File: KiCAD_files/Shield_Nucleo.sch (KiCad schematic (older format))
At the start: 125 parts, among them J1 Conn_01x02, J2 RJ45_LED_Shielded, J3 RJ45_LED_Shielded, J4 Conn_01x03_Male, J5 Conn_01x05_Male, J6 Conn_01x02, J7 Power, J8 Conn_02x07_Odd_Even, SW1 SW_Push, U1 STM32G474RE, U2 AT25xxx, U3 TCAN334GDR, U4 AP1117-33, U5 UCC21222DR, U6 UCC21222DR, U7 SFH617A-2X009T, U8 RFM-0505s, U9 RFM-0505s, Y1 NX3225SA-16.000000MHZ-T1

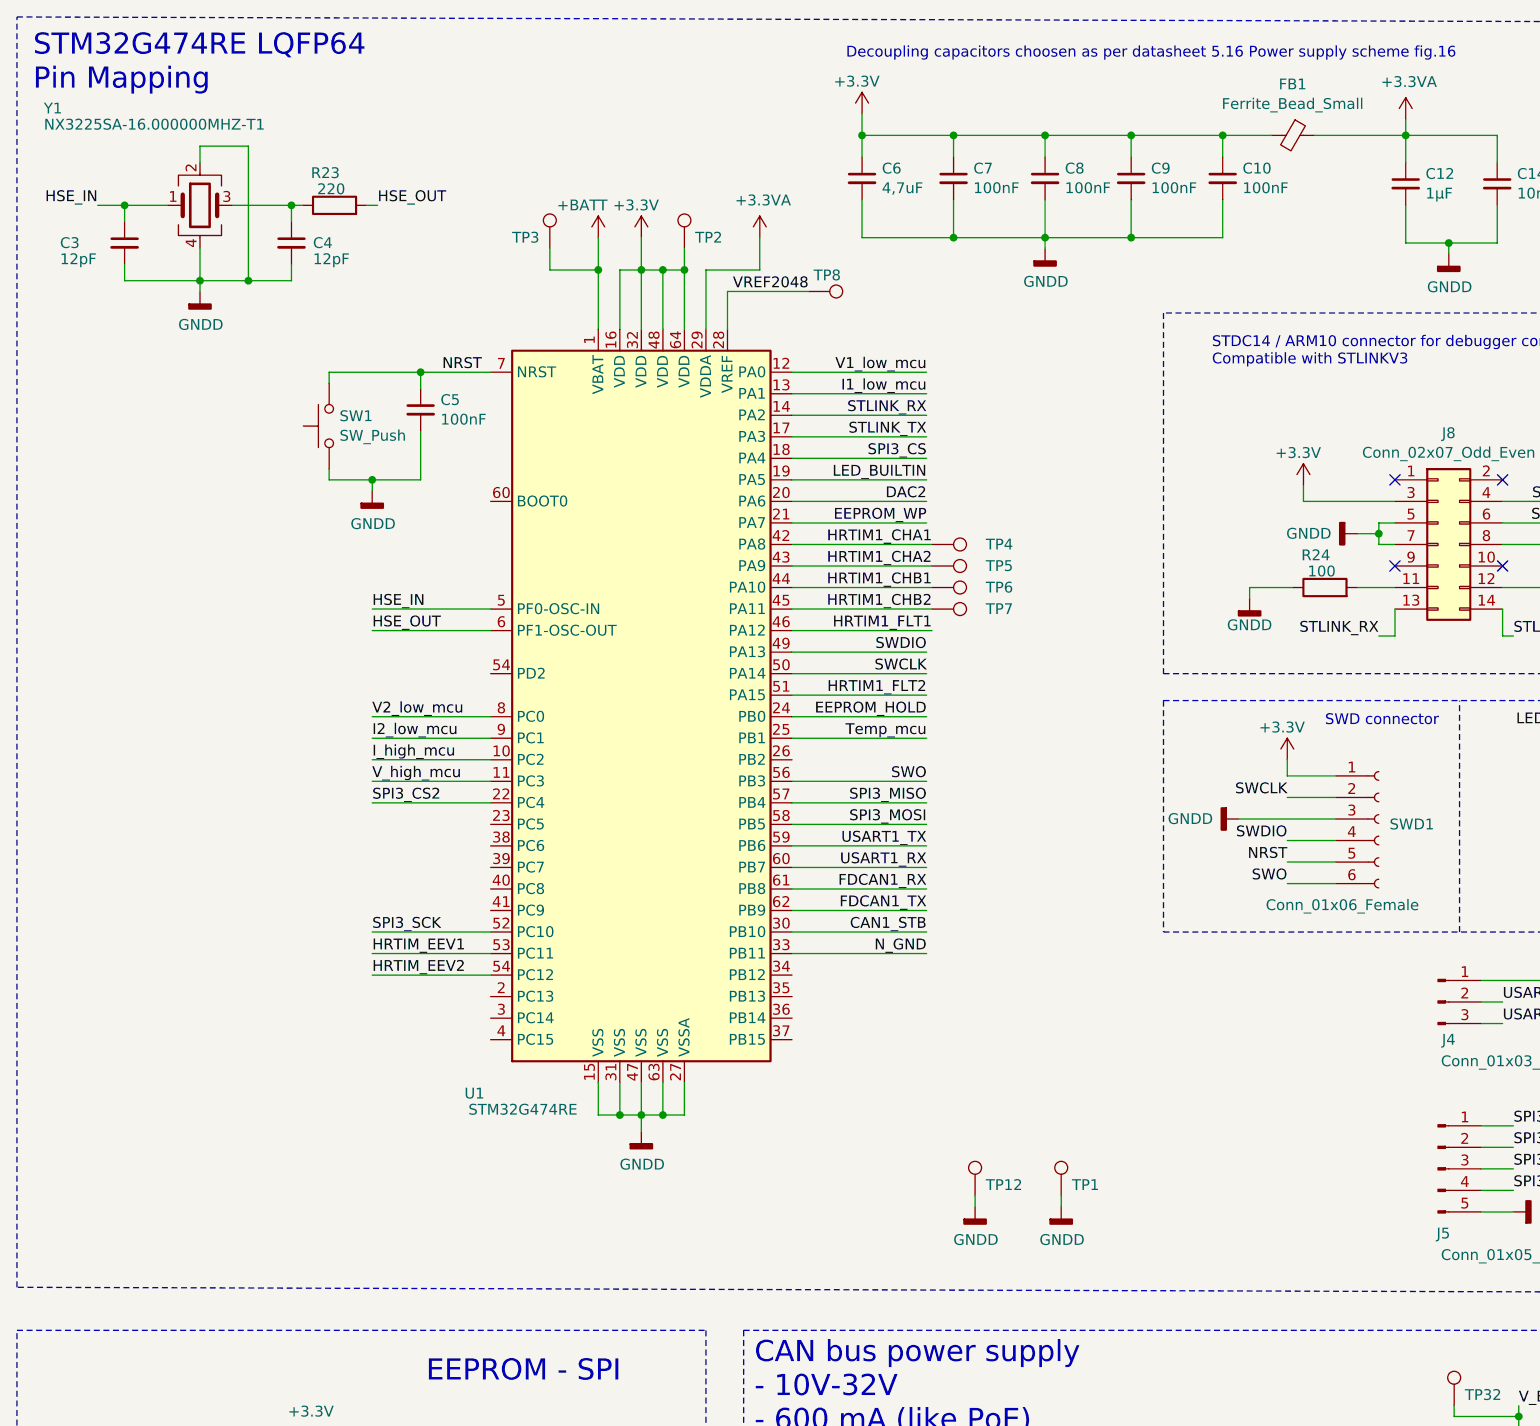
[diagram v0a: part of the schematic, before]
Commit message: WIP : Changed HSE from 16Mhz to 24Mhz to match nucleo design.
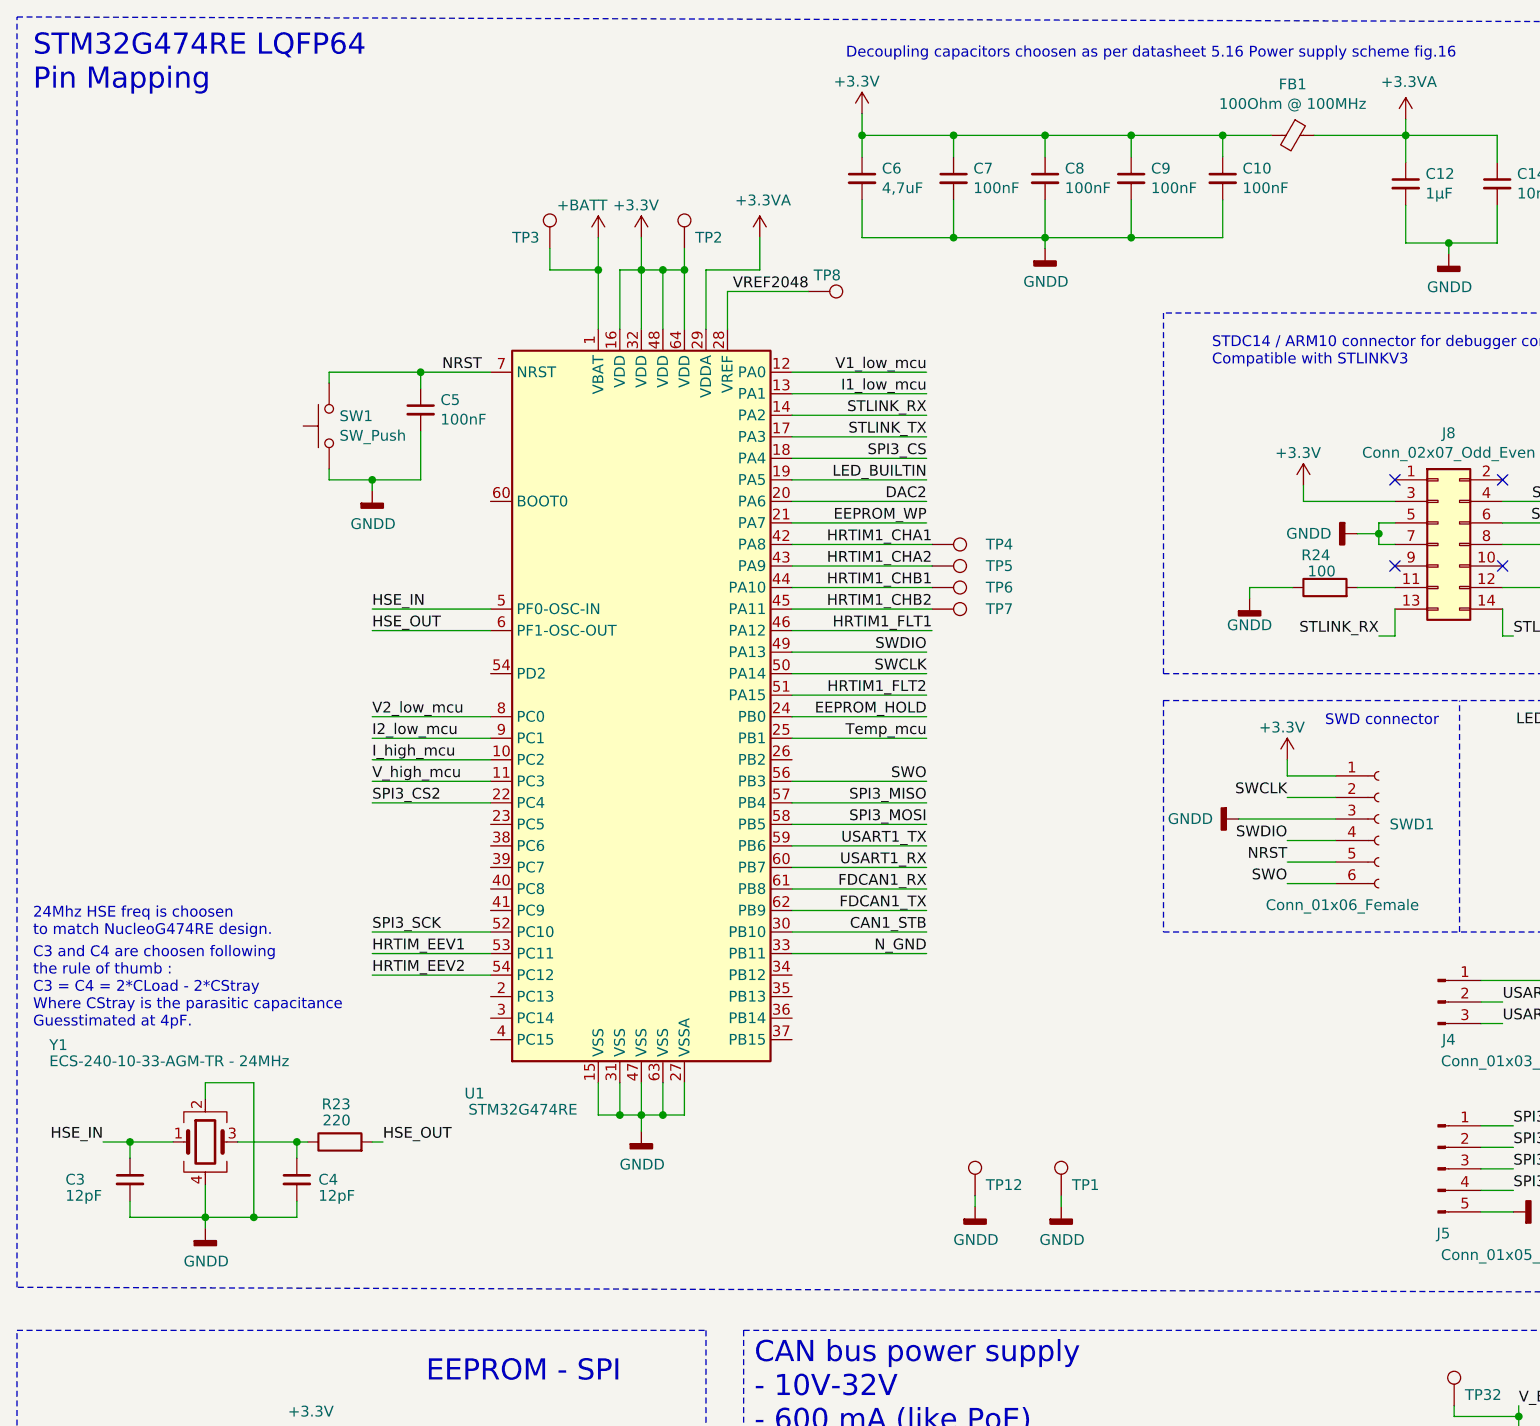
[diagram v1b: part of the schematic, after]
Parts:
- FB1: value Ferrite_Bead_Small -> 100Ohm @ 100MHz
- Y1: value NX3225SA-16.000000MHZ-T1 -> ECS-240-10-33-AGM-TR - 24MHz
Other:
- note added: "24Mhz HSE freq is choosen\nto match NucleoG474RE design."
- note added: "C3 and C4 are choosen following \nthe rule of thumb : \nC3 = C4 = 2*CLoad - 2*CStray \nWhere CStray is the parasitic capacitance\nGuesstimated at 4pF."
- moved on the sheet: C3, C4, R23, Y1
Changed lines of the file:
@@
 P 6725 1175
 F 0 "FB1" V 6488 1175 50  0000 C CNN
-F 1 "Ferrite_Bead_Small" V 6579 1175 50  0000 C CNN
+F 1 "100Ohm @ 100MHz" V 6579 1175 50  0000 C CNN
 F 2 "Resistor_SMD:R_0805_2012Metric" V 6655 1175 50  0001 C CNN
 F 3 "~" H 6725 1175 50  0001 C CNN
@@
 L Device:C_Small C3
 U 1 1 6110106A
-P 1300 1675
-F 0 "C3" H 1000 1675 50  0000 L CNN
-F 1 "12pF" H 1000 1600 50  0000 L CNN
-F 2 "Capacitor_SMD:C_0805_2012Metric" H 1300 1675 50  0001 C CNN
-F 3 "~" H 1300 1675 50  0001 C CNN
-	1    1300 1675
+P 1325 6025
+F 0 "C3" H 1025 6025 50  0000 L CNN
+F 1 "12pF" H 1025 5950 50  0000 L CNN
+F 2 "Capacitor_SMD:C_0805_2012Metric" H 1325 6025 50  0001 C CNN
+F 3 "~" H 1325 6025 50  0001 C CNN
+	1    1325 6025
 	1    0    0    -1
 $EndComp
@@
 L Device:C_Small C4
 U 1 1 6118360F
-P 2075 1675
-F 0 "C4" H 2175 1675 50  0000 L CNN
-F 1 "12pF" H 2175 1600 50  0000 L CNN
-F 2 "Capacitor_SMD:C_0805_2012Metric" H 2075 1675 50  0001 C CNN
-F 3 "~" H 2075 1675 50  0001 C CNN
-	1    2075 1675
+P 2100 6025
+F 0 "C4" H 2200 6025 50  0000 L CNN
+F 1 "12pF" H 2200 5950 50  0000 L CNN
+F 2 "Capacitor_SMD:C_0805_2012Metric" H 2100 6025 50  0001 C CNN
+F 3 "~" H 2100 6025 50  0001 C CNN
+	1    2100 6025
 	1    0    0    -1
 $EndComp
@@
 L power:GNDD #PWR01
 U 1 1 611DFE7E
-P 1650 1900
-F 0 "#PWR01" H 1650 1650 50  0001 C CNN
-F 1 "GNDD" H 1654 1745 50  0000 C CNN
-F 2 "" H 1650 1900 50  0001 C CNN
-F 3 "" H 1650 1900 50  0001 C CNN
-	1    1650 1900
-	1    0    0    -1
-$EndComp
-Wire Wire Line
-	1650 1850 1650 1900
+P 1675 6250
+F 0 "#PWR01" H 1675 6000 50  0001 C CNN
+F 1 "GNDD" H 1679 6095 50  0000 C CNN
+F 2 "" H 1675 6250 50  0001 C CNN
+F 3 "" H 1675 6250 50  0001 C CNN
+	1    1675 6250
+	1    0    0    -1
+$EndComp
+Wire Wire Line
+	1675 6200 1675 6250
 $Comp
 L power:GNDD #PWR05
@@
 L Device:Crystal_GND24 Y1
 U 1 1 62A5FC15
-P 1650 1500
-F 0 "Y1" H 925 1950 50  0000 L CNN
-F 1 "NX3225SA-16.000000MHZ-T1 " H 925 1875 50  0000 L CNN
-F 2 "Crystal:Crystal_SMD_3225-4Pin_3.2x2.5mm" H 1650 1500 50  0001 C CNN
-F 3 "~" H 1650 1500 50  0001 C CNN
-	1    1650 1500
-	1    0    0    -1
-$EndComp
-Wire Wire Line
-	1300 1775 1300 1850
-Wire Wire Line
-	1300 1850 1650 1850
-Wire Wire Line
-	2075 1850 2075 1775
-Wire Wire Line
-	1650 1850 1875 1850
-Connection ~ 1650 1850
-Wire Wire Line
-	1650 1700 1650 1850
-Wire Wire Line
-	1300 1575 1300 1500
-Wire Wire Line
-	1300 1500 1500 1500
-Wire Wire Line
-	1800 1500 2075 1500
-Wire Wire Line
-	2075 1500 2075 1575
-Wire Wire Line
-	1650 1300 1650 1225
-Wire Wire Line
-	1650 1225 1875 1225
-Wire Wire Line
-	1875 1225 1875 1850
-Connection ~ 1875 1850
-Wire Wire Line
-	1875 1850 2075 1850
+P 1675 5850
+F 0 "Y1" H 950 6300 50  0000 L CNN
+F 1 "ECS-240-10-33-AGM-TR   - 24MHz" H 950 6225 50  0000 L CNN
+F 2 "Crystal:Crystal_SMD_3225-4Pin_3.2x2.5mm" H 1675 5850 50  0001 C CNN
+F 3 "https://www.mouser.fr/datasheet/2/122/ecx-32-1100709.pdf" H 1675 5850 50  0001 C CNN
+	1    1675 5850
+	1    0    0    -1
+$EndComp
+Wire Wire Line
+	1325 6125 1325 6200
+Wire Wire Line
+	1325 6200 1675 6200
+Wire Wire Line
+	2100 6200 2100 6125
+Wire Wire Line
+	1675 6200 1900 6200
+Connection ~ 1675 6200
+Wire Wire Line
+	1675 6050 1675 6200
+Wire Wire Line
+	1325 5925 1325 5850
+Wire Wire Line
+	1325 5850 1525 5850
+Wire Wire Line
+	1825 5850 2100 5850
+Wire Wire Line
+	2100 5850 2100 5925
+Wire Wire Line
+	1675 5650 1675 5575
+Wire Wire Line
+	1675 5575 1900 5575
+Wire Wire Line
+	1900 5575 1900 6200
+Connection ~ 1900 6200
+Wire Wire Line
+	1900 6200 2100 6200
 Text Label 2450 3375 0    50   ~ 0
 HSE_IN
@@
 Wire Wire Line
 	2450 3375 3000 3375
-Text Label 1175 1500 2    50   ~ 0
+Text Label 1200 5850 2    50   ~ 0
 HSE_IN
-Text Label 2475 1500 0    50   ~ 0
+Text Label 2500 5850 0    50   ~ 0
 HSE_OUT
 Wire Wire Line
-	2125 1500 2075 1500
-Connection ~ 2075 1500
-Wire Wire Line
-	1175 1500 1300 1500
-Connection ~ 1300 1500
+	2150 5850 2100 5850
+Connection ~ 2100 5850
+Wire Wire Line
+	1200 5850 1325 5850
+Connection ~ 1325 5850
 $Comp
 L Device:R R23
 U 1 1 634D9AA5
-P 2275 1500
-F 0 "R23" V 2425 1475 50  0000 L CNN
-F 1 "220" V 2350 1450 50  0000 L CNN
-F 2 "Resistor_SMD:R_0805_2012Metric" V 2205 1500 50  0001 C CNN
-F 3 "~" H 2275 1500 50  0001 C CNN
-	1    2275 1500
+P 2300 5850
+F 0 "R23" V 2475 5800 50  0000 L CNN
+F 1 "220" V 2400 5800 50  0000 L CNN
+F 2 "Resistor_SMD:R_0805_2012Metric" V 2230 5850 50  0001 C CNN
+F 3 "~" H 2300 5850 50  0001 C CNN
+	1    2300 5850
 	0    -1   -1   0
 $EndComp
 Wire Wire Line
-	2425 1500 2475 1500
+	2450 5850 2500 5850
 Text Label 5025 3675 2    50   ~ 0
 SWCLK
@@
 Wire Wire Line
 	7600 6175 7750 6175
+Text Notes 875  5325 0    50   ~ 0
+C3 and C4 are choosen following \nthe rule of thumb : \nC3 = C4 = 2*CLoad - 2*CStray \nWhere CStray is the parasitic capacitance\nGuesstimated at 4pF.
+Text Notes 875  4900 0    50   ~ 0
+24Mhz HSE freq is choosen\nto match NucleoG474RE design.
 $EndSCHEMATC

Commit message: WIP: added extra comments
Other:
- note added: "I1 is tied to PC1 which is \nADC2 CH2 or \nCOMP1 INP (in current mode)"
- note added: "I2 is tied to PC1 which is ADC1 CH7 or \nCOMP3 INP (in current mode)"
- moved on the sheet: LED1, R28, SWD1
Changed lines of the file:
@@
 L Connector:Conn_01x06_Female SWD1
 U 1 1 643AFACC
-P 7125 4350
-F 0 "SWD1" H 7175 4325 50  0000 L CNN
-F 1 "Conn_01x06_Female" H 6600 3950 50  0000 L CNN
-F 2 "Connector_PinHeader_2.54mm:PinHeader_1x06_P2.54mm_Vertical" H 7125 4350 50  0001 C CNN
-F 3 "~" H 7125 4350 50  0001 C CNN
-	1    7125 4350
+P 7325 4350
+F 0 "SWD1" H 7375 4325 50  0000 L CNN
+F 1 "Conn_01x06_Female" H 6800 3950 50  0000 L CNN
+F 2 "Connector_PinHeader_2.54mm:PinHeader_1x06_P2.54mm_Vertical" H 7325 4350 50  0001 C CNN
+F 3 "~" H 7325 4350 50  0001 C CNN
+	1    7325 4350
 	1    0    0    -1
 $EndComp
@@
 L power:+3.3V #PWR038
 U 1 1 64438AFE
-P 6700 4075
-F 0 "#PWR038" H 6700 3925 50  0001 C CNN
-F 1 "+3.3V" H 6675 4225 50  0000 C CNN
-F 2 "" H 6700 4075 50  0001 C CNN
-F 3 "" H 6700 4075 50  0001 C CNN
-	1    6700 4075
-	1    0    0    -1
-$EndComp
-Wire Wire Line
-	6700 4075 6700 4150
-Wire Wire Line
-	6700 4150 6925 4150
-Text Label 6700 4250 2    50   ~ 0
+P 6900 4075
+F 0 "#PWR038" H 6900 3925 50  0001 C CNN
+F 1 "+3.3V" H 6875 4225 50  0000 C CNN
+F 2 "" H 6900 4075 50  0001 C CNN
+F 3 "" H 6900 4075 50  0001 C CNN
+	1    6900 4075
+	1    0    0    -1
+$EndComp
+Wire Wire Line
+	6900 4075 6900 4150
+Wire Wire Line
+	6900 4150 7125 4150
+Text Label 6900 4250 2    50   ~ 0
 SWCLK
 Wire Wire Line
-	6700 4250 6925 4250
+	6900 4250 7125 4250
 $Comp
 L power:GNDD #PWR036
 U 1 1 645B9E89
-P 6475 4350
-F 0 "#PWR036" H 6475 4100 50  0001 C CNN
-F 1 "GNDD" V 6475 4125 50  0000 C CNN
-F 2 "" H 6475 4350 50  0001 C CNN
-F 3 "" H 6475 4350 50  0001 C CNN
-	1    6475 4350
+P 6675 4350
+F 0 "#PWR036" H 6675 4100 50  0001 C CNN
+F 1 "GNDD" V 6675 4125 50  0000 C CNN
+F 2 "" H 6675 4350 50  0001 C CNN
+F 3 "" H 6675 4350 50  0001 C CNN
+	1    6675 4350
 	0    1    1    0
 $EndComp
 Wire Wire Line
-	6925 4350 6475 4350
-Text Label 6700 4450 2    50   ~ 0
+	7125 4350 6675 4350
+Text Label 6900 4450 2    50   ~ 0
 SWDIO
 Wire Wire Line
-	6700 4450 6925 4450
-Text Label 6700 4550 2    50   ~ 0
+	6900 4450 7125 4450
+Text Label 6900 4550 2    50   ~ 0
 NRST
 Wire Wire Line
-	6925 4550 6700 4550
-Text Label 6700 4650 2    50   ~ 0
+	7125 4550 6900 4550
+Text Label 6900 4650 2    50   ~ 0
 SWO
 Wire Wire Line
-	6925 4650 6700 4650
-Text Notes 6875 3925 0    50   ~ 0
+	7125 4650 6900 4650
+Text Notes 7075 3925 0    50   ~ 0
 SWD connector\n
 Wire Notes Line
-	7500 4875 7500 3800
-Wire Notes Line
-	6125 3800 6125 4875
+	7700 4875 7700 3800
+Wire Notes Line
+	6275 3800 6275 4875
 Wire Wire Line
 	7200 3500 7200 3375
@@
 	6525 3275 6725 3275
 Wire Notes Line
-	6125 3675 8750 3675
+	6275 3675 8750 3675
 Wire Notes Line
 	8750 3675 8750 2000
 Wire Notes Line
-	8750 2000 6125 2000
-Wire Notes Line
-	6125 2000 6125 3675
+	8750 2000 6275 2000
+Wire Notes Line
+	6275 2000 6275 3675
 Text Notes 6350 2250 0    50   ~ 0
 STDC14 / ARM10 connector for debugger connection\nCompatible with STLINKV3\n
@@
 Text Label 5025 2775 2    50   ~ 0
 LED_BUILTIN
-Text Label 8200 3925 2    50   ~ 0
-LED_BUILTIN
-$Comp
-L Device:LED LED1
-U 1 1 61233B4F
-P 8200 4125
-F 0 "LED1" V 8239 4007 50  0000 R CNN
-F 1 "LED" V 8148 4007 50  0000 R CNN
-F 2 "LED_SMD:LED_0805_2012Metric" H 8200 4125 50  0001 C CNN
-F 3 "~" H 8200 4125 50  0001 C CNN
-	1    8200 4125
-	0    -1   -1   0
-$EndComp
-$Comp
-L Device:R R28
-U 1 1 6129C61B
-P 8200 4475
-F 0 "R28" H 8270 4521 50  0000 L CNN
-F 1 "330" H 8270 4430 50  0000 L CNN
-F 2 "Resistor_SMD:R_0805_2012Metric" V 8130 4475 50  0001 C CNN
-F 3 "~" H 8200 4475 50  0001 C CNN
-	1    8200 4475
-	1    0    0    -1
-$EndComp
-Wire Wire Line
-	8200 4275 8200 4325
-Wire Wire Line
-	8200 3925 8200 3975
-$Comp
-L power:GNDD #PWR041
-U 1 1 61392ABD
-P 8200 4675
-F 0 "#PWR041" H 8200 4425 50  0001 C CNN
-F 1 "GNDD" H 8204 4520 50  0000 C CNN
-F 2 "" H 8200 4675 50  0001 C CNN
-F 3 "" H 8200 4675 50  0001 C CNN
-	1    8200 4675
-	1    0    0    -1
-$EndComp
-Wire Wire Line
-	8200 4625 8200 4675
 Wire Notes Line
 	8750 3800 8750 4875
 Wire Notes Line
-	6125 4875 8750 4875
-Wire Notes Line
-	6125 3800 8750 3800
+	6275 4875 8750 4875
+Wire Notes Line
+	6275 3800 8750 3800
 $Comp
 L Symbols:RFM-0505s U8
@@
 Text Notes 875  4900 0    50   ~ 0
 24Mhz HSE freq is choosen\nto match NucleoG474RE design.
+Text Notes 850  4050 0    50   ~ 0
+I2 is tied to PC1 which is ADC1 CH7 or \nCOMP3 INP (in current mode)
+Text Notes 5075 2550 0    50   ~ 0
+I1 is tied to PC1 which is \nADC2 CH2 or \nCOMP1 INP (in current mode)
+Wire Wire Line
+	8400 4625 8400 4675
+$Comp
+L power:GNDD #PWR041
+U 1 1 61392ABD
+P 8400 4675
+F 0 "#PWR041" H 8400 4425 50  0001 C CNN
+F 1 "GNDD" H 8404 4520 50  0000 C CNN
+F 2 "" H 8400 4675 50  0001 C CNN
+F 3 "" H 8400 4675 50  0001 C CNN
+	1    8400 4675
+	1    0    0    -1
+$EndComp
+Wire Wire Line
+	8400 3925 8400 3975
+Wire Wire Line
+	8400 4275 8400 4325
+$Comp
+L Device:R R28
+U 1 1 6129C61B
+P 8400 4475
+F 0 "R28" H 8470 4521 50  0000 L CNN
+F 1 "330" H 8470 4430 50  0000 L CNN
+F 2 "Resistor_SMD:R_0805_2012Metric" V 8330 4475 50  0001 C CNN
+F 3 "~" H 8400 4475 50  0001 C CNN
+	1    8400 4475
+	1    0    0    -1
+$EndComp
+$Comp
+L Device:LED LED1
+U 1 1 61233B4F
+P 8400 4125
+F 0 "LED1" V 8439 4007 50  0000 R CNN
+F 1 "LED" V 8348 4007 50  0000 R CNN
+F 2 "LED_SMD:LED_0805_2012Metric" H 8400 4125 50  0001 C CNN
+F 3 "~" H 8400 4125 50  0001 C CNN
+	1    8400 4125
+	0    -1   -1   0
+$EndComp
+Text Label 8400 3925 2    50   ~ 0
+LED_BUILTIN
 $EndSCHEMATC

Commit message: Added missing references
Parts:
- BT1: Manf# (none) -> 97384199
- C1, C10, C11, C13, C2, C20, C21, C22, C25, C26, C30, C31, C32, C5, C7, C8, C9: Manf# (none) -> CC0805KRX7R9BB104
- C12, C23, C33: Manf# (none) -> CL21B105KBFNFNE
- C14: Manf# (none) -> C0805X103K5RAC3316
- C15, C16: value CP1_Small -> 47uF; Manf# (none) -> 865080645012
- C17, C18, C27, C28: Manf# (none) -> C0805C330J5GACTU
- C19, C24, C34, C35, C36, C37, C38, C39, C40: Manf# (none) -> CL32B106KBJZW6E
- C29: value 10 to 47uF -> 10uF; Manf# (none) -> EEE-FN2A100P
- C3, C4: Manf# (none) -> C0805C120K5HACTU
- C6: Manf# (none) -> CGA4J1X7R1H475K125AE
- D1, D2: value RBR2MM60BTFTR -> RBR2MM60ATFTR; Manf# (none) -> RBR2MM60ATFTR
- D10, D11: Manf# (none) -> STTH4R02U
- D3, D4, D5, D6, D7, D8, D9: Manf# (none) -> MMSZ5226C-HE3-08
- F1, F2: Manf# (none) -> 0ZCJ0050AF2E
- FB1: Manf# (none) -> ILBB0805ER101V
- J1, J6: Manf# (none) -> 1814919
- J2, J3: Manf# (none) -> RJE721881411
- J4: Manf# (none) -> TSW-103-07-T-S
- J5: Manf# (none) -> TSW-105-07-T-S
- J7, JP1, JP3, JP4: DNP (none) -> x
- J8: Manf# (none) -> FTSH-107-01-F-DV-K
- JP2: Manf# (none) -> TSW-102-07-T-S
- LED1: Manf# (none) -> 150080RS75000
- PS4: Manf# (none) -> PQDE6W-Q110-S5-D
- PS5: Manf# (none) -> VXO78012-500-M-TR
- R1: Manf# (none) -> CR0805-FX-1200ELF
- R10, R12, R28: Manf# (none) -> CRCW0805330RFKEAC
- R11, R13: Manf# (none) -> CR0805-FX-3001ELF
- R14, R17, R18, R21, R9: Manf# (none) -> RT0805FRE0751RL
- R15, R19, R2, R25, R3, R4, R5, R6, R7, R8: Manf# (none) -> PCF-W0805LF-03-2002-B-P-LT
- R16, R20: Manf# (none) -> CR0805AF/-2R20EAS
- R22: Manf# (none) -> RC0805FR-071KL
- R23: Manf# (none) -> CRCW0805220RFKEAC
- R24: Manf# (none) -> CR0805-FX-1000ELF
- R26, R27: Manf# (none) -> APC0805B100KN
- SW1: Manf# (none) -> KMR241NGLFS
- SWD1: Manf# (none) -> TSW-106-07-T-S
- TH1: Manf# (none) -> NXFT15XH103FA2B100
- TP1, TP12, TP13, TP14, TP15, TP2, TP3, TP32, TP33, TP4, TP5, TP6, TP7, TP8: Manf# (none) -> 5001
- U1: Manf# (none) -> STM32G474RE
- U2: Manf# (none) -> AT25256B-SSPDGV-T
- U3: Manf# (none) -> TCAN334GDR
- U4: Manf# (none) -> AP1117E33G-13
- U5, U6: Manf# (none) -> UCC21222DR
- U7: Manf# (none) -> SFH617A-2X009T
- U8, U9: Manf# (none) -> ROE0505S
- Y1: Manf# (none) -> ECS-240-10-33-AGM-TR
